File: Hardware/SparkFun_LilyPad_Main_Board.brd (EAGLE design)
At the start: 50 x 50 mm, 39 parts, among them U1 ATMEGA328P_TQFP, Y1 8MHZ

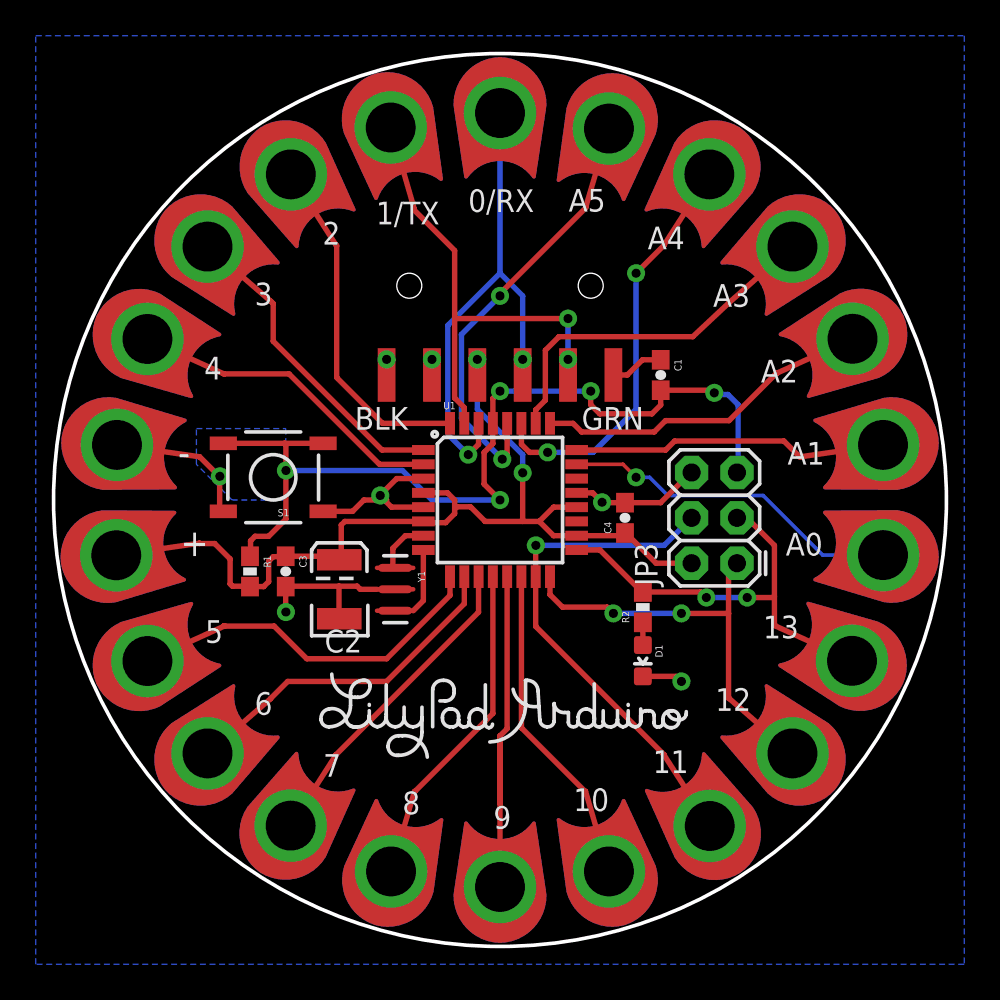
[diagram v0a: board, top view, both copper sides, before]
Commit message: Updates for QC checklist
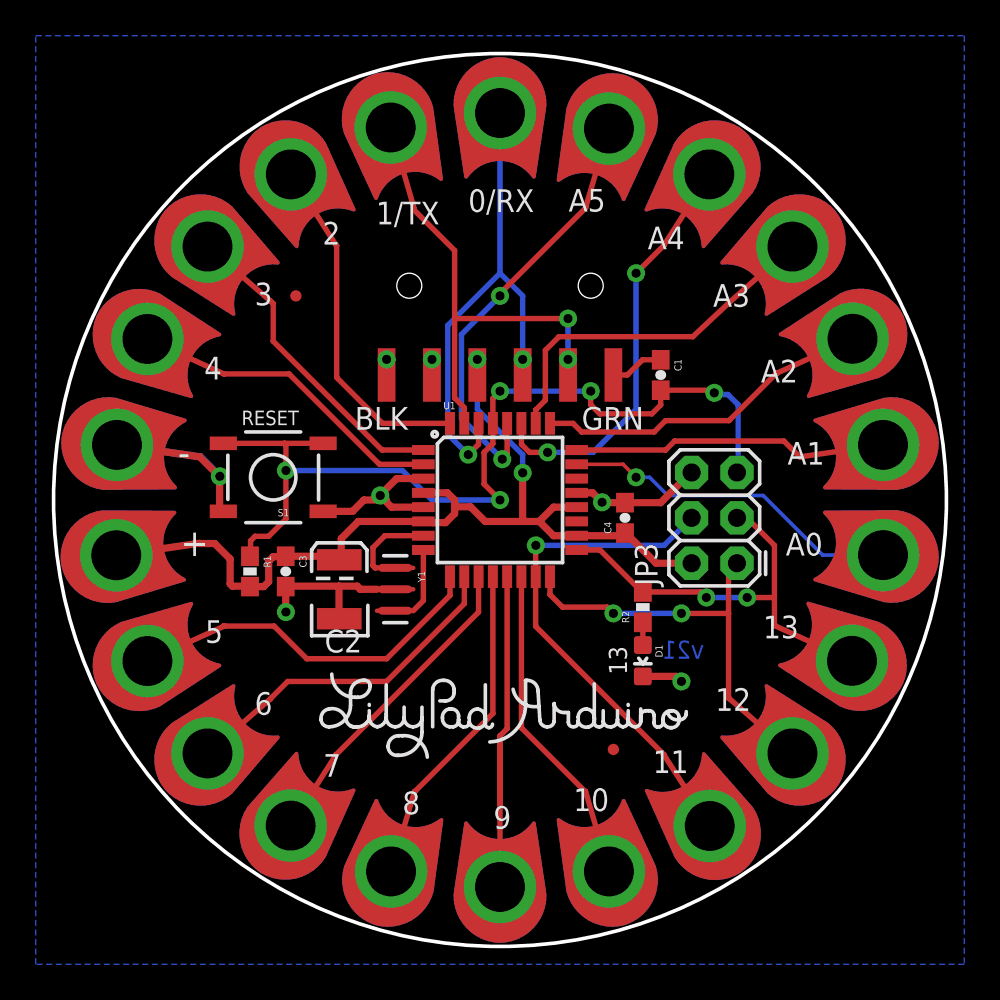
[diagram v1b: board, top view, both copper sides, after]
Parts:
- added FID1, FID2: FIDUCIALUFIDUCIAL, SparkFun-Aesthetics:MICRO-FIDUCIAL
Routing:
- net GND: track 38.0 -> 44.3 mm
- net N$1: track 3.15 -> 4.38 mm
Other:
- board text added: "Board thickness : .031""
- board text added: "RESET"
- board text added: "dimensions in inches"
- board text added: "v21"

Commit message: Moving logos to bottom copper, removed some silk
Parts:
- JP3: device SparkFun-Connectors:2X3 -> SparkFun-Connectors:2X3-NS
- LOGO1: value SFE_LOGO_FLAME.3_INCH -> SFE_LOGO_FLAME.3COP; device SparkFun-Aesthetics:SFE_LOGO_FLAME_.3 -> SparkFun-Aesthetics:SFE_LOGO_FLAME_COPPER_.3
- LOGO2: value OSHW-LOGOL -> OSHW-LOGO-COPPERM; device SparkFun-Aesthetics:OSHW-LOGO-L -> SparkFun-Aesthetics:OSHW-LOGO-M
- moved JP3 2.84 mm to (12.0, -1.00)
- moved LOGO1 1.27 mm to (5.08, -14.0)
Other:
- board text added: "B"
- board text added: "G"
- board text removed: "BLK"
- board text removed: "GRN"
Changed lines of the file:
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@@
 <layer number="45" name="Holes" color="7" fill="1" visible="yes" active="yes"/>
 <layer number="46" name="Milling" color="3" fill="1" visible="no" active="yes"/>
-<layer number="47" name="Measures" color="7" fill="1" visible="yes" active="yes"/>
+<layer number="47" name="Measures" color="7" fill="1" visible="no" active="yes"/>
 <layer number="51" name="tDocu" color="6" fill="1" visible="yes" active="yes"/>
 <layer number="3" name="Route3" color="4" fill="3" visible="no" active="no"/>
@@
 <text x="8.89" y="-36.83" size="1.778" layer="51" font="vector">L. Buechley</text>
 <text x="26.67" y="-36.83" size="1.778" layer="51" font="vector">N. Seidle</text>
-<text x="-8.128" y="3.937" size="1.27" layer="21" font="vector" ratio="12">BLK</text>
-<text x="4.572" y="3.937" size="1.27" layer="21" font="vector" ratio="12">GRN</text>
 <polygon width="0.5" layer="42">
 <vertex x="-4" y="18.7"/>
@@
 <text x="-6.35" y="-44.45" size="1.778" layer="47" font="vector" ratio="15">dimensions in inches</text>
 <text x="-17.78" y="27.94" size="1.778" layer="51" font="vector" ratio="15">Board thickness : .031"</text>
-<text x="7.112" y="-9.779" size="1.016" layer="21" font="vector" ratio="15" rot="R90">13</text>
+<text x="7.112" y="-9.779" size="0.8128" layer="21" font="vector" ratio="15" rot="R90">13</text>
 <text x="-14.478" y="4.191" size="0.8128" layer="21" font="vector" ratio="15">RESET</text>
+<text x="-6.985" y="3.302" size="1.016" layer="21" font="vector" ratio="15">B</text>
+<text x="5.715" y="3.302" size="1.016" layer="21" font="vector" ratio="15">G</text>
 </plain>
 <attributes>
@@
 <element name="U$1" library="LilyPad-Wearables" package="PETAL-LONG-1-2SIDE" value="SEWTAP9" x="21.48" y="-3.09" rot="R171.8"/>
 <element name="$0000003" library="LilyPad-Wearables" package="LOGO-LPA" value="LOGO-LPLPA" x="0" y="-11.7"/>
-<element name="JP3" library="SparkFun-Connectors" package="2X3" value="FEMALE 2x3" x="13.27" y="-3.54" rot="R90"/>
-<element name="C2" library="SparkFun-Capacitors" package="EIA3528" value="47uF" x="-9" y="-5" rot="R90">
+<element name="JP3" library="SparkFun-Connectors" package="2X3-NS" value="FEMALE 2x3" x="12" y="-1" smashed="yes" rot="R90">
+<attribute name="NAME" x="7.555" y="-2.27" size="1.27" layer="25" ratio="10" rot="R90"/>
+<attribute name="VALUE" x="15.175" y="-2.27" size="1.27" layer="27" rot="R90"/>
+</element>
+<element name="C2" library="SparkFun-Capacitors" package="EIA3528" value="47uF" x="-9" y="-5" smashed="yes" rot="R90">
 <attribute name="PROD_ID" value="CAP-08310" x="-9" y="-5" size="1.778" layer="27" rot="R90" display="off"/>
 <attribute name="VALUE" value="47uF" x="-9" y="-5" size="1.778" layer="27" rot="R90" display="off"/>
+<attribute name="NAME" x="-7.73" y="-7.27" size="1.27" layer="25" rot="R180"/>
+<attribute name="VALUE" x="-7.63" y="-1.76" size="1.27" layer="27" rot="R180"/>
 </element>
 <element name="C3" library="SparkFun-Capacitors" package="0603-CAP" value="1.0uF" x="-12" y="-4" rot="R270">
@@
 <attribute name="VALUE" value="1.0uF" x="-12" y="-4" size="1.778" layer="27" rot="R270" display="off"/>
 </element>
-<element name="Y1" library="SparkFun-FreqCtrl" package="RESONATOR-SMD" value="8MHZ" x="-5.873" y="-5" rot="R270">
+<element name="Y1" library="SparkFun-FreqCtrl" package="RESONATOR-SMD" value="8MHZ" x="-5.873" y="-5" smashed="yes" rot="R270">
 <attribute name="PROD_ID" value="XTAL-08895" x="-5.873" y="-5" size="1.778" layer="27" rot="R270" display="off"/>
 <attribute name="VALUE" value="8MHZ" x="-5.873" y="-5" size="1.778" layer="27" rot="R270" display="off"/>
+<attribute name="NAME" x="-4.603" y="-3.984" size="0.4064" layer="25" rot="R270"/>
+<attribute name="VALUE" x="-7.4605" y="-4.0475" size="0.4064" layer="27" rot="R270"/>
 </element>
 <element name="JP1" library="SparkFun-Connectors" package="1X06-SMD" value="" x="0" y="12" rot="R180">
@@
 <attribute name="VALUE" value="0.1uF" x="9" y="7" size="1.778" layer="27" rot="R270" display="off"/>
 </element>
-<element name="LOGO1" library="SparkFun-Aesthetics" package="SFE_LOGO_FLAME_.3" value="SFE_LOGO_FLAME.3_INCH" x="6.35" y="-13.97" rot="MR0"/>
-<element name="LOGO2" library="SparkFun-Aesthetics" package="OSHW-LOGO-L" value="OSHW-LOGOL" x="-3.81" y="-11.43" rot="MR0"/>
-<element name="S1" library="SparkFun-Electromechanical" package="TACTILE-SWITCH-SMD" value="SWITCH-MOMENTARY-2SMD-REDUNDANT" x="-12.7" y="1.27" rot="R180">
+<element name="LOGO1" library="SparkFun-Aesthetics" package="SFE_LOGO_FLAME_COPPER_.3" value="SFE_LOGO_FLAME.3COP" x="5.08" y="-13.97" rot="MR0"/>
+<element name="LOGO2" library="SparkFun-Aesthetics" package="OSHW-LOGO-M" value="OSHW-LOGO-COPPERM" x="-3.81" y="-11.43" rot="MR0"/>
+<element name="S1" library="SparkFun-Electromechanical" package="TACTILE-SWITCH-SMD" value="SWITCH-MOMENTARY-2SMD-REDUNDANT" x="-12.7" y="1.27" smashed="yes" rot="R180">
 <attribute name="PROD_ID" value="SWCH-08247" x="-12.7" y="1.27" size="1.778" layer="27" font="vector" ratio="15" rot="R180" display="off"/>
+<attribute name="NAME" x="-11.811" y="-0.508" size="0.4064" layer="25" rot="R180"/>
+<attribute name="VALUE" x="-11.811" y="3.302" size="0.4064" layer="27" rot="R180"/>
 </element>
 <element name="FRAME1" library="SparkFun-Aesthetics" package="CREATIVE_COMMONS" value="" x="-19.539478125" y="-36.83">

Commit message: Made pin 13 LED blue; current standard
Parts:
- D1: value GREEN -> BLUE
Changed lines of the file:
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@@
 <element name="U$7" library="LilyPad-Wearables" package="PETAL-LONG-1-2SIDE" value="SEWTAP9" x="0" y="21.7" rot="R270"/>
 <element name="U$14" library="LilyPad-Wearables" package="PETAL-LONG-1-2SIDE" value="SEWTAP9" x="-11.74" y="-18.26" rot="R57.3"/>
-<element name="D1" library="SparkFun-LED" package="LED-0603" value="GREEN" x="8" y="-9" rot="R180">
-<attribute name="PROD_ID" value="DIO-00821" x="8" y="-9" size="1.778" layer="27" rot="R180" display="off"/>
-<attribute name="VALUE" value="GREEN" x="8" y="-9" size="1.778" layer="27" rot="R180" display="off"/>
+<element name="D1" library="SparkFun-LED" package="LED-0603" value="BLUE" x="8" y="-9" rot="R180">
+<attribute name="PROD_ID" value="DIO-08575" x="8" y="-9" size="1.778" layer="27" rot="R180" display="off"/>
+<attribute name="VALUE" value="BLUE" x="8" y="-9" size="1.778" layer="27" rot="R180" display="off"/>
 </element>
 <element name="R2" library="SparkFun-Resistors" package="0603-RES" value="330" x="8" y="-6" rot="R90">
